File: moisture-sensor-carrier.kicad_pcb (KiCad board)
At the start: 4 copper layers, 42 x 155 mm, 61 parts, among them J1 USB-C receptacle, J2 Battery - Adafruit 1578, J3 Solar panel, J4 SWD 10p 1.27mm, J5 U.FL-R-SMT-1(10) antenna, U1 nRF54L15-QFAA, U2 nPM1300-QEAA, U3 FDC1004, U4 SHT45-AD1F, U5 TPS7A1650 5V LDO, X1 CM8V-T1A 32.768kHz CL=7pF 20p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, X2 FA-128 32MHz CL=8pF

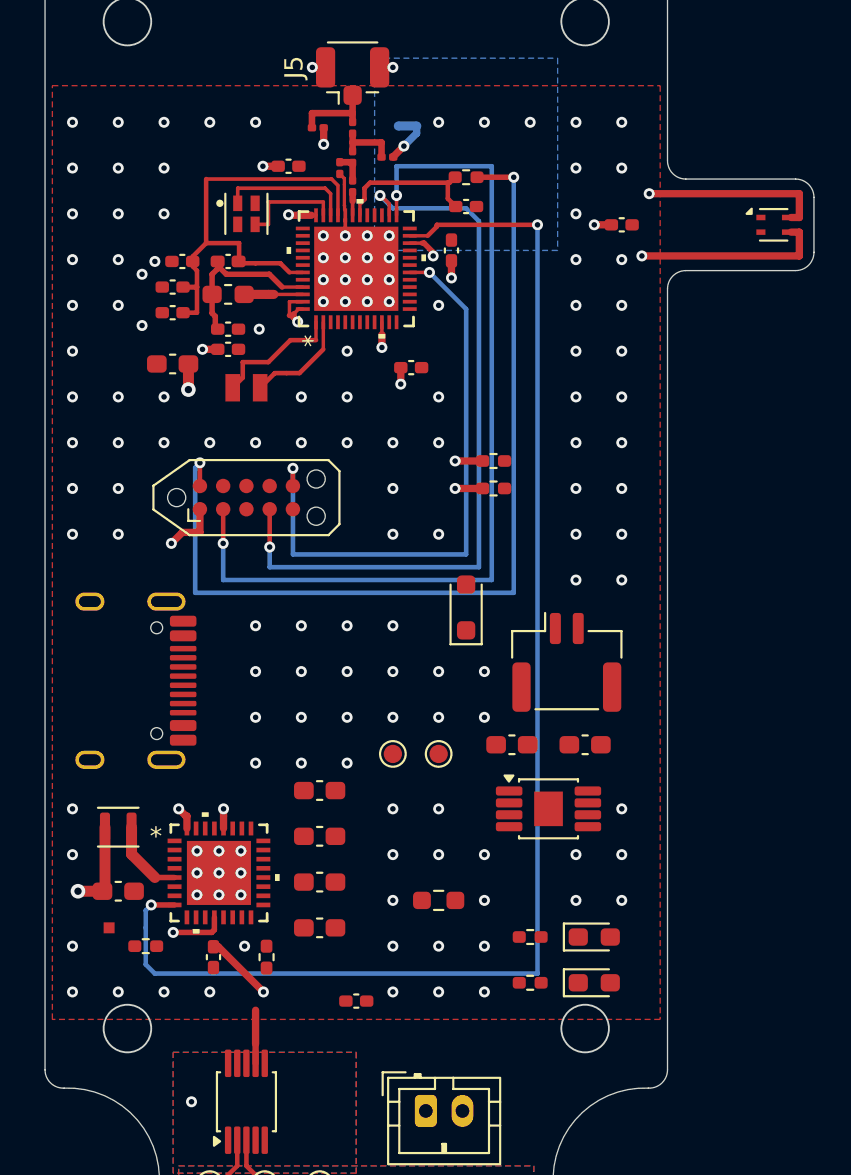
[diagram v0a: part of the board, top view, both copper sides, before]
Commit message: Consolidate moisture sensor PCB design and BOM
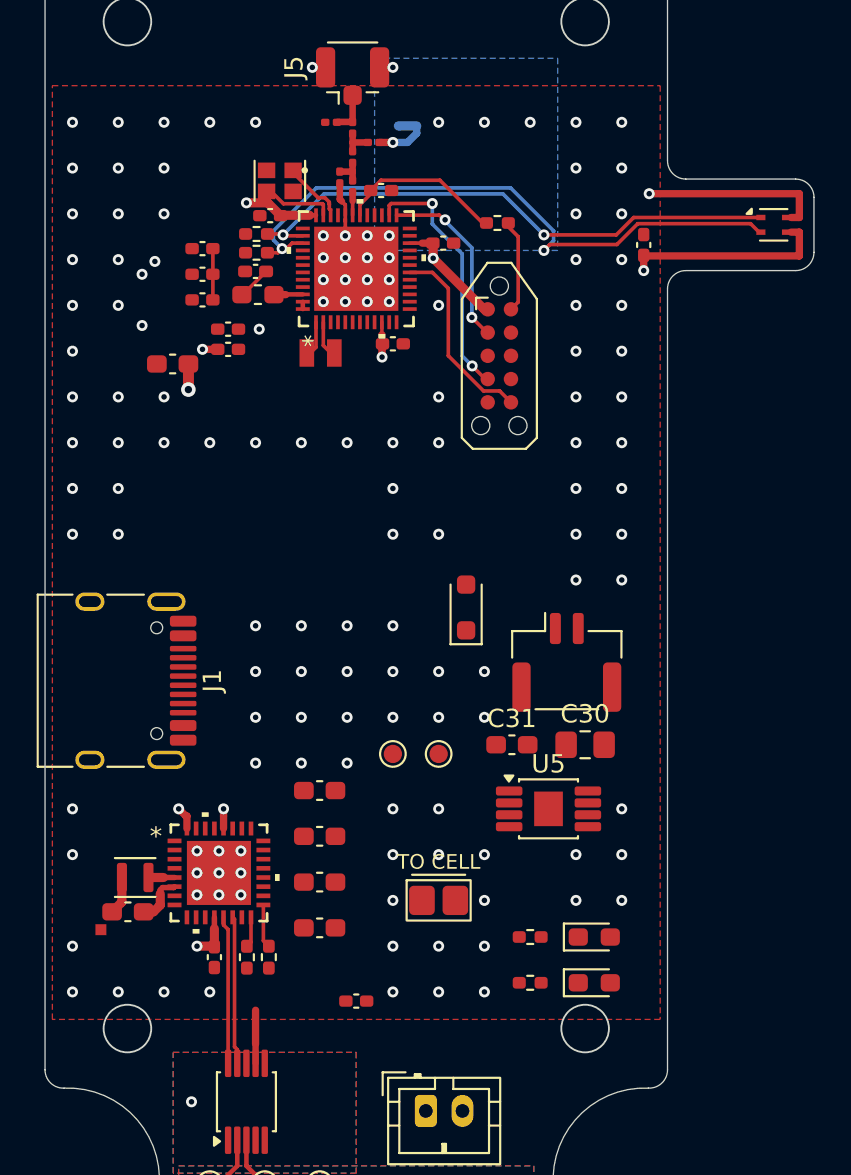
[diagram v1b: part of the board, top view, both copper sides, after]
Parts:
- C30: footprint C_0603_1608Metric_Pad1.08x0.95mm_HandSolder -> C_0805_2012Metric_Pad1.18x1.45mm_HandSolder
- C31: footprint C_0603_1608Metric_Pad1.08x0.95mm_HandSolder -> Capacitor_SMD:C_0603_1608Metric_Pad1.08x0.95mm_HandSolder
- C6: value 1.5pF GJM0335C1E1R5WB01 -> 1.5pF
- C9: value 2.0pF GJM0335C1E2R0WB01 -> 2.0pF
- J5: footprint U.FL_Hirose_U.FL-R-SMT-1_Vertical -> Connector_Coaxial:U.FL_Hirose_U.FL-R-SMT-1_Vertical
- L1: value MLZ1608M4R7WT000 4.7uH -> 4.7uH
- L10: value 2.2uH Isat>350mA DCR<400m -> 2.2uH Isat>350mA
- L2: value 2.7nH LQP03HQ2N7B02 -> 2.7nH
- L3, L4: value 3.5nH LQP03HQ3N5B02 -> 3.5nH
- TH1: footprint Resistor_SMD:R_0603_1608Metric_Pad0.98x0.95mm_HandSolder -> Thermistor_SEMITEC_103JT_Wired
- U5: footprint HVSSOP-8-1EP_3x3mm_P0.65mm_EP1.57x1.89mm -> Package_SO:HVSSOP-8-1EP_3x3mm_P0.65mm_EP1.57x1.89mm
- moved R23 18.3 mm to (71.5, 62.1)
- moved R22 17.9 mm to (71.6, 61.1)
- moved J4 15.8 mm to (84.8, 67.8), turned to -90 degrees
- moved R20 5.56 mm to (71.0, 100.6), turned to -90 degrees
- moved C13 4.72 mm to (78.4, 58.7)
- moved X1 4.47 mm to (75.0, 67.6)
- moved R1 3.03 mm to (84.7, 60.5)
- moved L10 2.90 mm to (64.9, 96.2)
- moved C4 2.88 mm to (72.3, 60.1), turned to 180 degrees
- moved X2 2.56 mm to (72.8, 58.2), turned to 180 degrees
- moved C12 1.77 mm to (68.6, 63.3)
- moved C5 1.77 mm to (68.6, 64.7)
- moved C8 1.64 mm to (79.0, 67.1)
- moved L1 1.63 mm to (71.6, 64.4)
- moved C27 1.63 mm to (92.7, 61.7), turned to 90 degrees
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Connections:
- U5 pad 2: (no net) -> unconnected-(U5-FB/DNC-Pad2)
- U5 pad 3: (no net) -> unconnected-(U5-PG-Pad3)
- U5 pad 6: (no net) -> unconnected-(U5-NC-Pad6)
- U5 pad 7: (no net) -> unconnected-(U5-DELAY-Pad7)
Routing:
- net /PMIC_INT: track 74.4 -> 0.00 mm, vias 2 -> 0
- net /SWD_RST: track 50.6 -> 4.89 mm, vias 2 -> 0
- net /SCL: track 0.00 -> 42.6 mm, vias 0 -> 2
- net /SWDIO: track 49.0 -> 9.87 mm
- net /SDA: track 0.00 -> 38.4 mm, vias 0 -> 2
- net /SWDCLK: track 40.8 -> 13.7 mm
- net /DECA: track 25.5 -> 2.80 mm
- net /P2.07_SWO: track 32.4 -> 10.6 mm, vias 2 -> 0
- net +3V3: track 44.0 -> 33.3 mm, vias 19 -> 9
- net /DECD: track 9.32 -> 1.80 mm
- net /XL1: track 7.10 -> 1.81 mm
- net /XC1: track 7.20 -> 3.15 mm
- net /XL2: track 5.80 -> 1.85 mm
- net /SW2: track 4.35 -> 1.42 mm
- net /GND_PVSS2: track 0.00 -> 2.74 mm
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
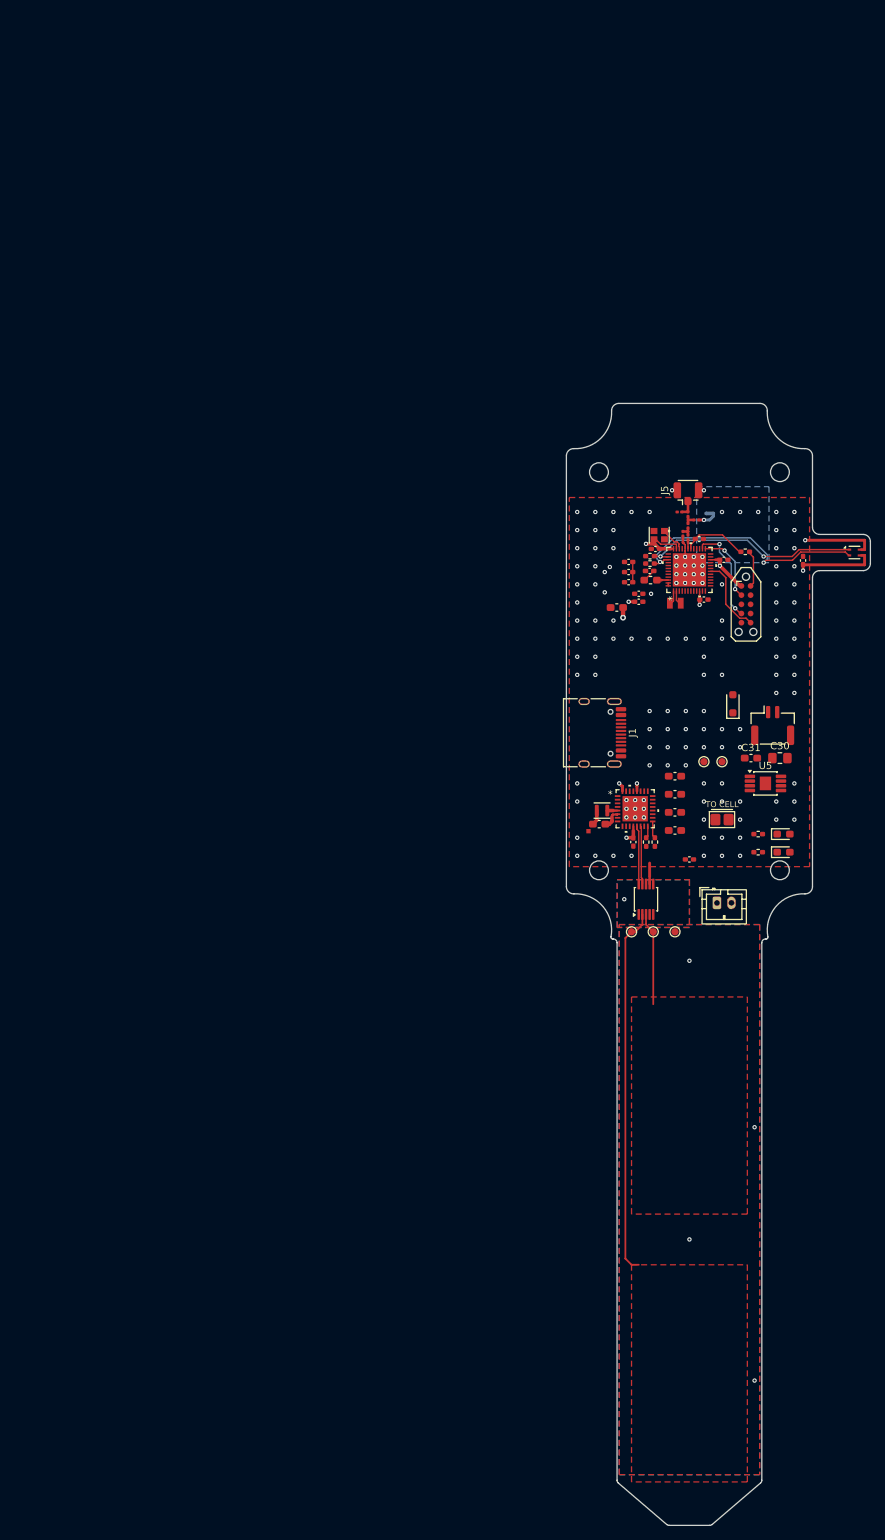
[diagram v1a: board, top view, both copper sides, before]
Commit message: Lock CR2032 mechanics and nPM2100 power layout
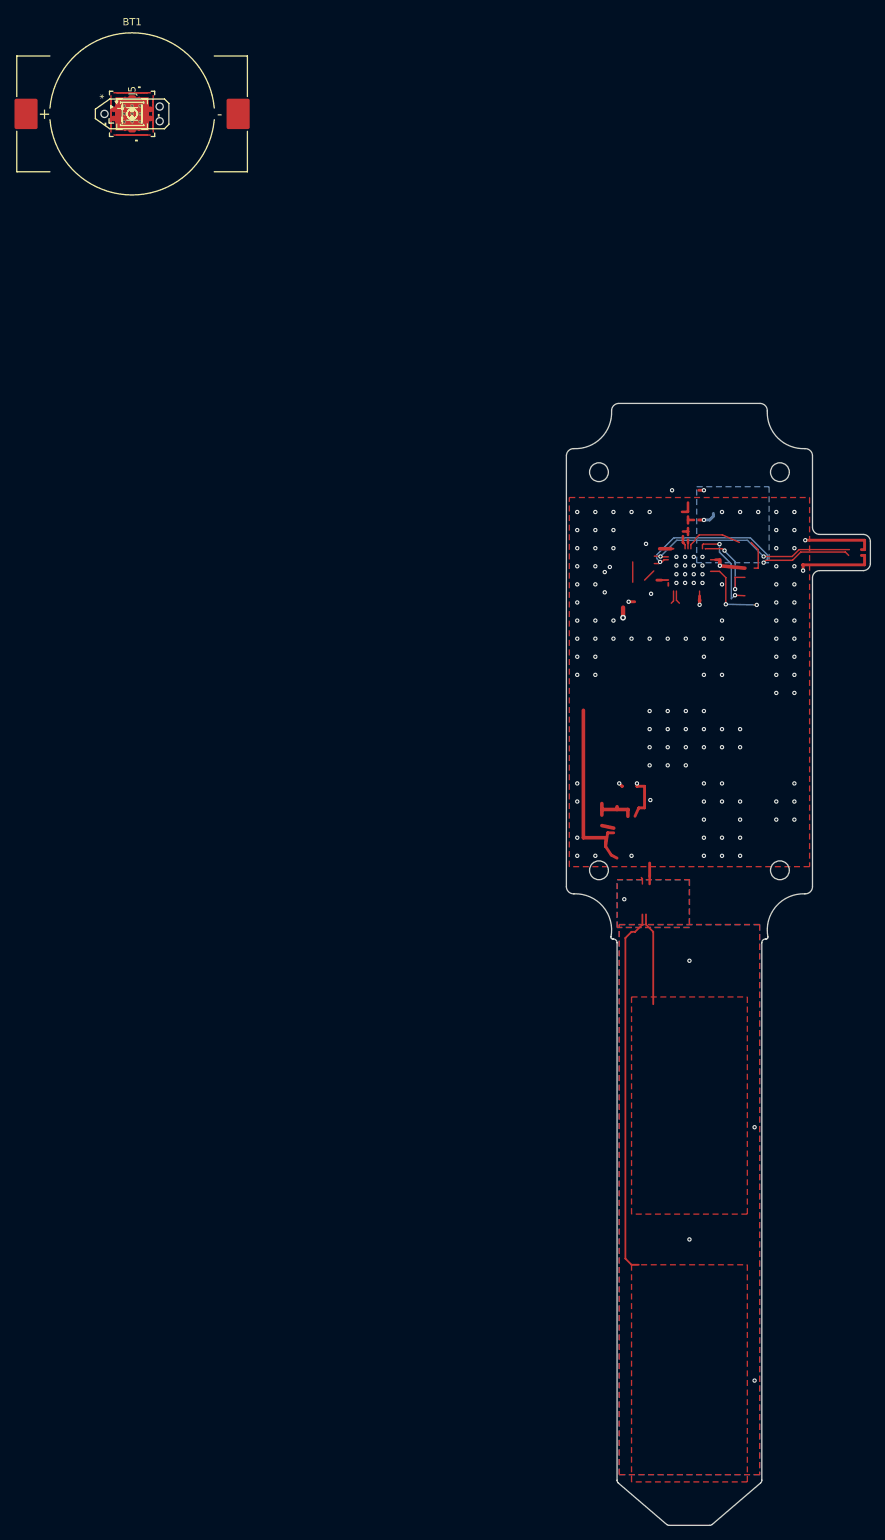
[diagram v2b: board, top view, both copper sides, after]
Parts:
- removed C20: 1uF/10V X5R, Capacitor_SMD:C_0603_1608Metric_Pad1.08x0.95mm_HandSolder
- removed C30: 4.7uF/50V X5R, C_0805_2012Metric_Pad1.18x1.45mm_HandSolder
- removed C31: 10uF/25V X5R, Capacitor_SMD:C_0603_1608Metric_Pad1.08x0.95mm_HandSolder
- removed D3: GREEN, LED_SMD:LED_0603_1608Metric_Pad1.05x0.95mm_HandSolder
- removed D4: RED, LED_SMD:LED_0603_1608Metric_Pad1.05x0.95mm_HandSolder
- removed D5: RB751V-40 Schottky, Diode_SMD:D_SOD-323_HandSoldering
- removed J1: USB-C receptacle, Connector_USB:USB_C_Receptacle_HRO_TYPE-C-31-M-12
- removed J2: Battery - Adafruit 1578, Connector_JST:JST_PH_B2B-PH-K_1x02_P2.00mm_Vertical
- removed J3: Solar panel, Connector_JST:JST_GH_SM02B-GHS-TB_1x02-1MP_P1.25mm_Horizontal
- removed MP1: Hammond_1551WKBK, Enclosure_1551WK
- removed NT3: GND_PVSS2 to GND (at the via), footprints:NetTie_Small
- removed R20: 470k 1% VSET2=3.3V, Resistor_SMD:R_0402_1005Metric_Pad0.72x0.64mm_HandSolder
- removed R21: 0R disables BUCK1, Resistor_SMD:R_0402_1005Metric_Pad0.72x0.64mm_HandSolder
- removed R25, R26: 1k, Resistor_SMD:R_0402_1005Metric_Pad0.72x0.64mm_HandSolder
- removed TH1: 10k B3435 - couple to cell, Thermistor_SEMITEC_103JT_Wired
- removed TP4: SHPHLD, TestPoint:TestPoint_Pad_D1.0mm
- removed TP5: SOLAR_5V, TestPoint:TestPoint_Pad_D1.0mm
- removed U5: TPS7A1650 5V LDO, Package_SO:HVSSOP-8-1EP_3x3mm_P0.65mm_EP1.57x1.89mm
- added BT1: BU2032SM-BT-GTR, footprints:BatteryHolder_MPD_BU2032SM-BT-GTR, F.Cu at (0.00, 0.00)
- C21: value 10uF/25V X5R -> 10uF/6.3V X5R; footprint Capacitor_SMD:C_0603_1608Metric_Pad1.08x0.95mm_HandSolder -> Capacitor_SMD:C_0402_1005Metric
- C22, C24: value 10uF/25V X5R -> 1nF X5R; footprint Capacitor_SMD:C_0603_1608Metric_Pad1.08x0.95mm_HandSolder -> Capacitor_SMD:C_0201_0603Metric
- C23: value 2.2uF/16V X7R -> 22uF/6.3V X5R; footprint Capacitor_SMD:C_0603_1608Metric_Pad1.08x0.95mm_HandSolder -> Capacitor_SMD:C_0402_1005Metric
- C25: value 100nF X5R -> 2.2uF/6.3V X5R; footprint Capacitor_SMD:C_0402_1005Metric_Pad0.74x0.62mm_HandSolder -> Capacitor_SMD:C_0402_1005Metric
- L10: value 2.2uH Isat>350mA -> 2.2uH 20% DFE201210U-2R2M=P2; footprint Inductor_SMD:L_Murata_DFE201610P -> footprints:IND_Murata_DFE201210U
- U2: value nPM1300-QEAA -> nPM2100-QEAA; footprint footprints:QFN32_5X5_NOR -> Package_DFN_QFN:QFN-16-1EP_4x4mm_P0.65mm_EP2.7x2.7mm_ThermalVias
- moved TP3 135.6 mm to (0.00, 0.00)
- moved TP2 134.0 mm to (0.00, 0.00)
- moved TP1 132.4 mm to (0.00, 0.00)
- moved U3 129.7 mm to (0.00, 0.00), turned to 0 degrees
- moved C26 128.6 mm to (0.00, 0.00)
- moved C23 124.2 mm to (0.00, 0.00)
- moved C22 122.2 mm to (0.00, 0.00)
- moved C25 122.1 mm to (0.00, 0.00), turned to 0 degrees
- moved C21 120.3 mm to (0.00, 0.00)
- moved U2 118.5 mm to (0.00, 0.00)
- moved C24 117.4 mm to (0.00, 0.00)
- moved U4 116.8 mm to (0.00, 0.00)
- moved L10 116.1 mm to (0.00, 0.00), turned to 0 degrees
- moved C27 111.4 mm to (0.00, 0.00), turned to 0 degrees
- moved J4 108.6 mm to (0.00, 0.00), turned to 0 degrees
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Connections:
- C21 pad 1: VSYS -> VBAT
- C22 pad 1: VSYS -> VBAT
- C23 pad 1: VBAT -> /VINT
- C24 pad 1: +3V3 -> /VINT
- C24 pad 2: /GND_PVSS2 -> GND
- L10 pad 1: /SW2 -> /SW
- L10 pad 2: +3V3 -> /VINT
- U2 pad 10: unconnected-(U2-GPIO3-Pad10) -> /SWD_RST
- U2 pad 11: unconnected-(U2-GPIO4-Pad11) -> GND
- U2 pad 12: +3V3 -> FDC_VDD
- U2 pad 13: /SDA -> +3V3
- U2 pad 14: /SCL -> /VINT
- U2 pad 15: /SHPHLD -> /VINT
- U2 pad 16: /VSET2 -> GND
- U2 pad 17: /VSET1 -> GND
- U2 pad 2: GND -> /SW
- U2 pad 3: unconnected-(U2-SW1-Pad3) -> VBAT
- U2 pad 4: VSYS -> unconnected-(U2-SHPHLD-Pad4)
- U2 pad 5: /SW2 -> /PMIC_INT
- U2 pad 6: /GND_PVSS2 -> /SDA
- U2 pad 7: unconnected-(U2-GPIO0-Pad7) -> /SCL
- U2 pad 8: /PMIC_INT -> GND
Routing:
- net VBAT: track 0.00 -> 26.9 mm
- net /SDA: track 38.4 -> 30.3 mm
- net /SCL: track 42.6 -> 35.4 mm
- net /VINT: track 0.00 -> 6.51 mm
- net /XC2: track 3.87 -> 0.00 mm
- net /XC1: track 3.15 -> 0.00 mm
- net /GND_PVSS2: track 2.74 -> 0.00 mm
- net +3V3: track 33.3 -> 30.7 mm, vias 9 -> 8
- net /VSET1: track 2.38 -> 0.00 mm
- net /SWDIO: track 9.87 -> 11.7 mm
- net /SW: track 0.00 -> 1.67 mm
- net /VSET2: track 1.67 -> 0.00 mm
- net /SW2: track 1.42 -> 0.00 mm
- net /NRESET: track 8.73 -> 7.98 mm
- net /P2.07_SWO: track 10.6 -> 10.8 mm, vias 0 -> 2
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
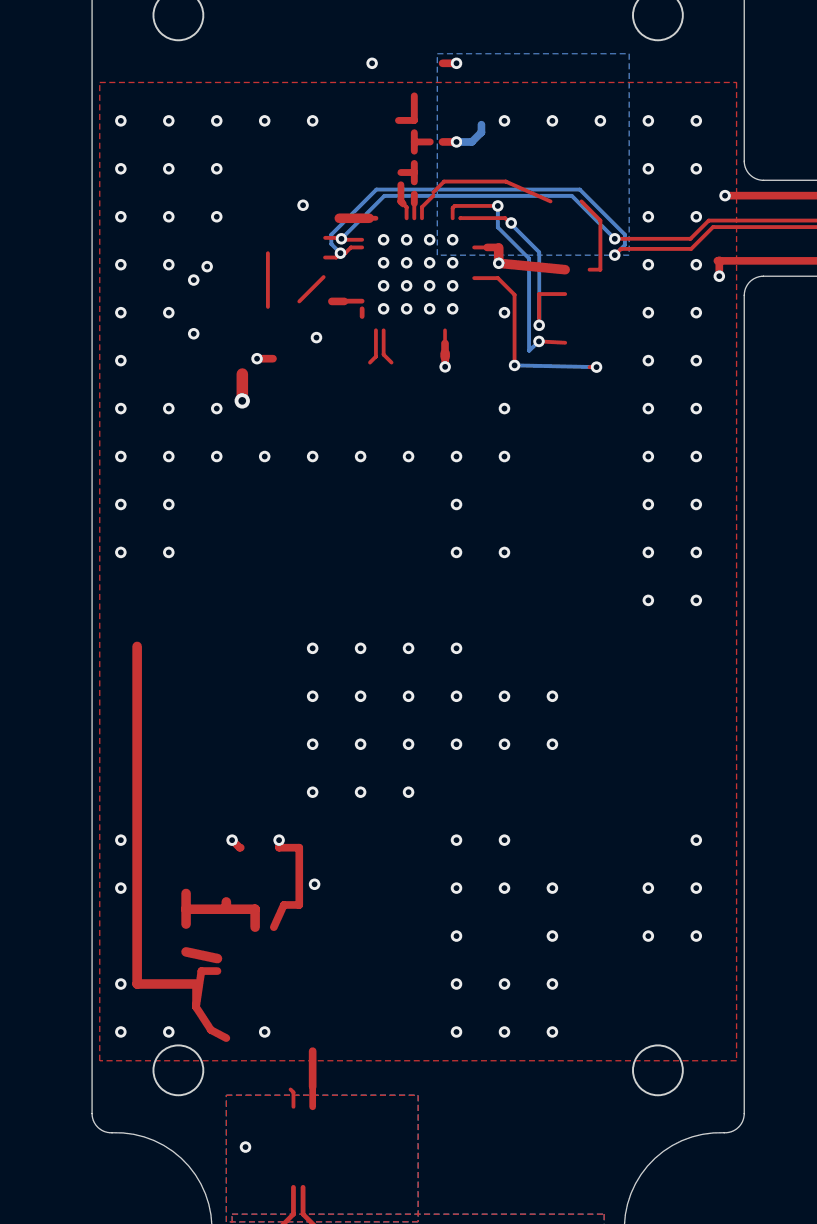
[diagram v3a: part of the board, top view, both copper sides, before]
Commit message: Clean PCB routing and retire fixed via stitching
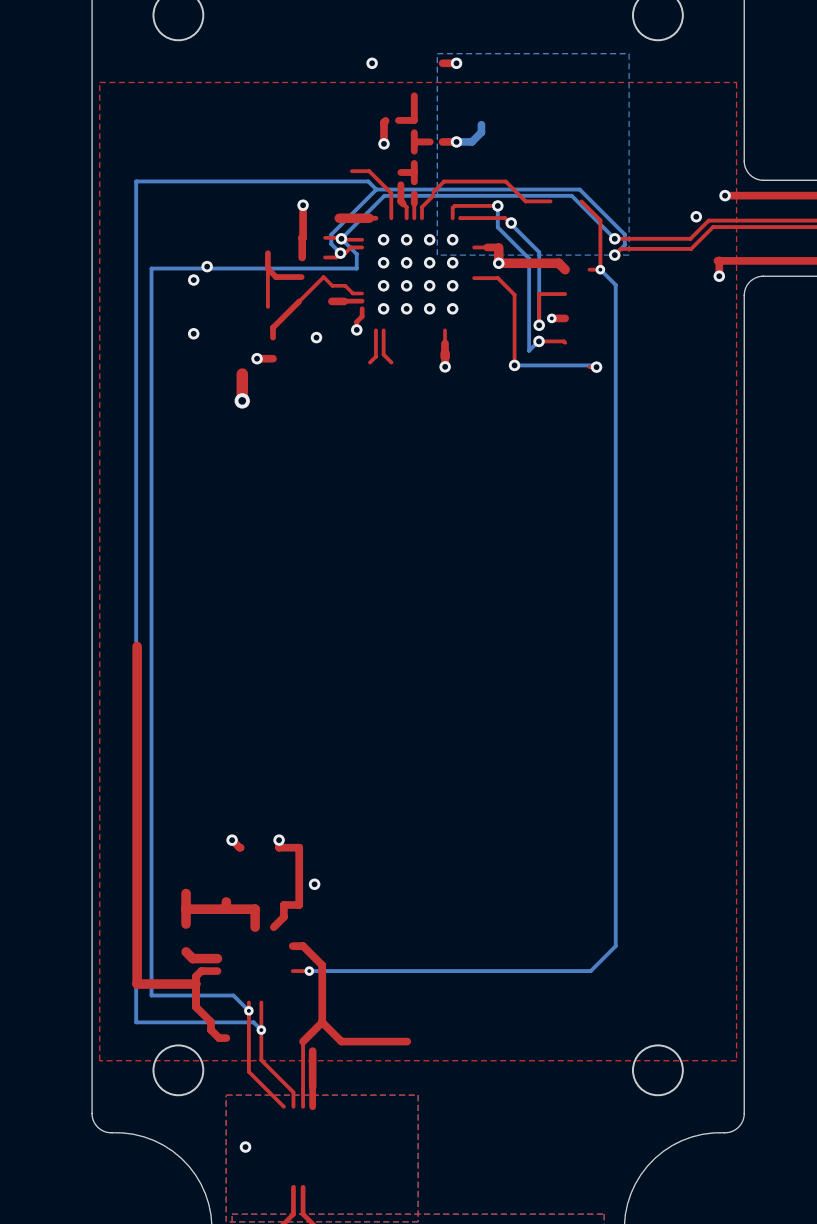
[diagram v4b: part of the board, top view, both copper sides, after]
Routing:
- net /SCL: track 35.4 -> 103.8 mm, vias 2 -> 3
- net /SDA: track 30.3 -> 92.4 mm, vias 2 -> 4
- net /SWD_RST: track 4.53 -> 57.5 mm, vias 0 -> 2
- net FDC_VDD: track 0.00 -> 14.6 mm
- net /DECD: track 1.80 -> 6.61 mm
- net /XC1: track 0.00 -> 3.83 mm
- net +3V3: track 30.7 -> 34.5 mm, vias 8 -> 9
- net /DECA: track 2.80 -> 5.55 mm
- net GND: track 13.6 -> 15.5 mm, vias 129 -> 26
